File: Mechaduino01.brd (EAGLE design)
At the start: 42.9 x 43.2 mm, 57 parts, among them IC1 SAMD21G18A-AUT, IC2 AP2112K-3.3, Q1 2.5A/30V, Q2 NFET, U3 74AHC1G125, Y1 32,768Khz

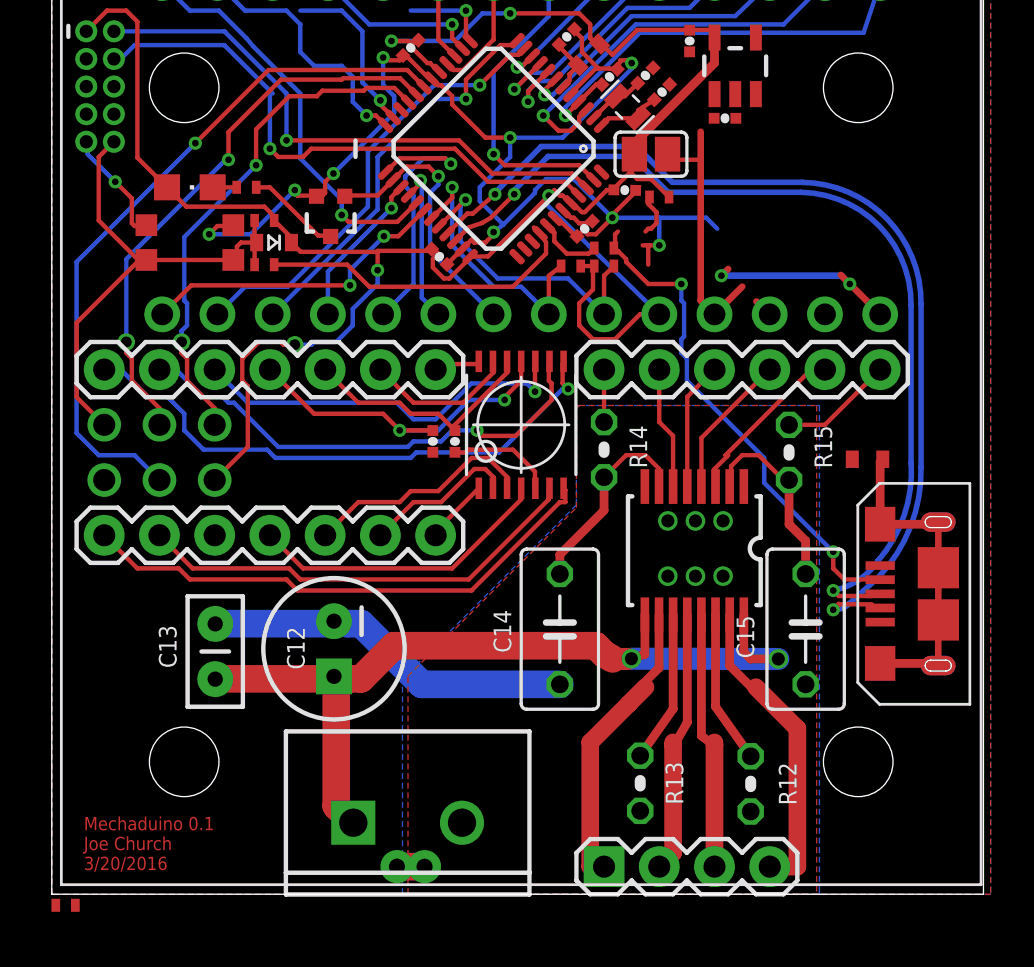
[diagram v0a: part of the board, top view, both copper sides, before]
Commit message: hardwired encoder, driver
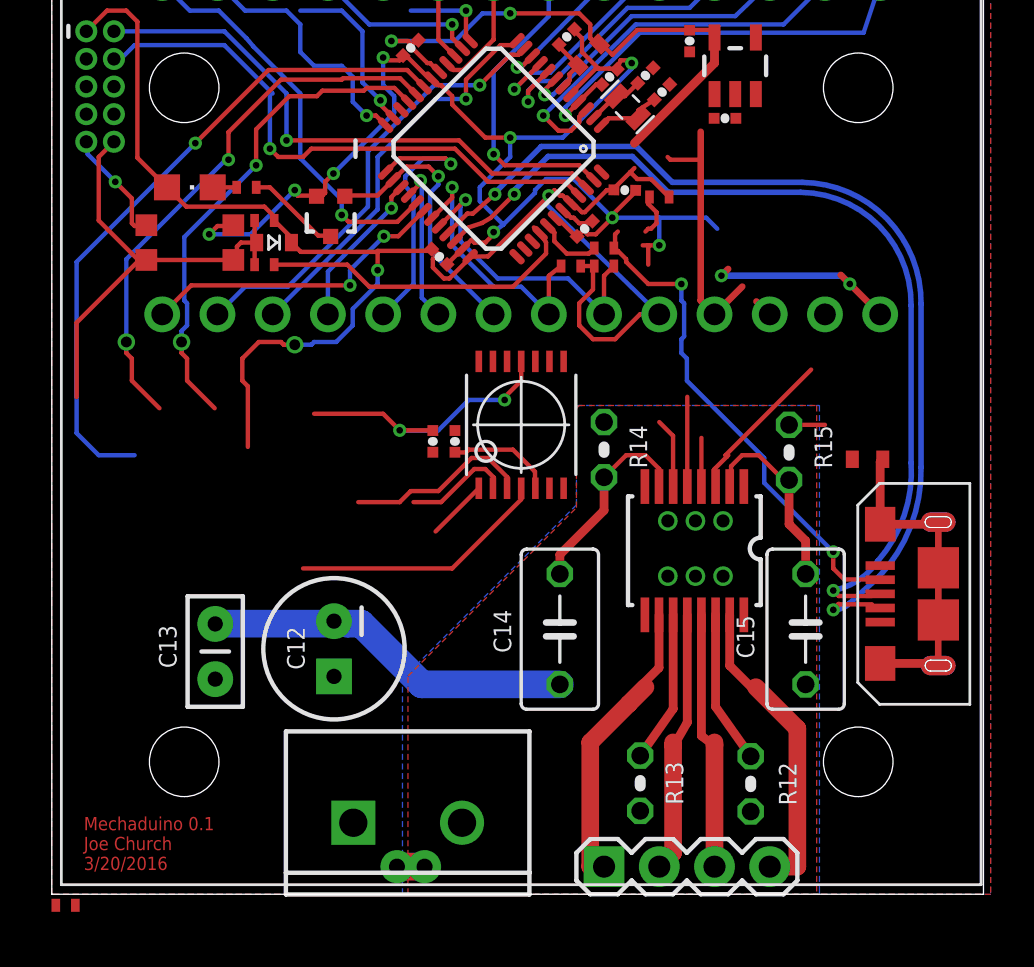
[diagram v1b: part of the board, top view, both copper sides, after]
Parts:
- removed JP10, JP11: (no value), SparkFun-Connectors:1X07
- removed JP3: SPI, Arduino-Neutrino-082:CONNETTORI_2X03
- removed JP5: (no value), SparkFun-Connectors:1X06
- removed SJ1: (no value), jumper:SJ
- renumbered POWERCONNECTOR to MOTOR_POWER
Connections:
- net N$5 renamed V+
- removed net ARDUINO_D4: IC1.13, JP1.12
- removed net ARDUINO_D5: IC1.24, JP1.13
- removed net ARDUINO_D6: IC1.29, JP1.14
- removed net ARDUINO_D7: IC1.30, JP2.1
- removed net ARDUINO_D8: IC1.11, JP2.2
- removed net ARDUINO_D9: IC1.12, JP2.3
- removed net N$10: JP5.4, U$1.5
- removed net N$11: JP5.5, U$1.6
- removed net N$12: JP5.6, R14.1
- removed net N$17: JP10.1, U$4.1
- removed net N$18: JP10.2, U$4.2
- removed net N$19: JP10.3, U$4.3
- removed net N$20: JP10.4, U$4.4
- removed net N$21: JP5.1, R15.1
- removed net N$22: JP10.6, U$4.6
- removed net N$23: JP10.7, U$4.7
- removed net N$24: JP11.1, U$4.8
- removed net N$25: JP11.2, U$4.9
- removed net N$26: JP11.3, U$4.10
- removed net N$28: C17.1, JP11.5, U$4.12
- removed net N$29: JP11.6, U$4.13
- removed net N$30: JP11.7, U$4.14
- removed net N$8: JP5.2, U$1.3
- removed net N$9: JP5.3, U$1.4
- removed net PB10_S4_SPI_MOSI: IC1.19, JP3.4
- removed net PB11_S4_SPI_SCK: IC1.20, JP3.3
- removed net PB12_S4_SPI_MISO: IC1.21, JP3.1
- new net ARDUINO_D4----VREF2: IC1.13, JP1.12, R15.1
- new net ARDUINO_D5----IN3: IC1.24, JP1.13, U$1.3
- new net ARDUINO_D6----IN4: IC1.29, JP1.14, U$1.4
- new net ARDUINO_D7----IN2: IC1.30, JP2.1, U$1.5
- new net ARDUINO_D8----IN1: IC1.11, JP2.2, U$1.6
- new net ARDUINO_D9----VREF1: IC1.12, JP2.3, R14.1
- new net HEADER_MISO: IC1.21, U$4.3
- new net HEADER_MOSI: IC1.19, U$4.4
- new net HEADER_SCK: IC1.20, U$4.2
- new net HEADER_SS: U$4.1
- net 3.3V: now also C17.1, U$4.12; no longer JP3.2, SJ1.2
- net GND: now also U$4.13; no longer JP10.5, JP3.6
- net N$27: no longer JP11.4
- net RESET: no longer JP3.5
- net VIN: no longer SJ1.1
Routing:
- net HEADER_MOSI: track 0.00 -> 42.8 mm, vias 0 -> 1
- net V+: track 39.8 -> 0.00 mm, vias 2 -> 0
- net PB10_S4_SPI_MOSI: track 32.5 -> 0.00 mm, vias 1 -> 0
- net HEADER_MISO: track 0.00 -> 31.6 mm, vias 0 -> 2
- net HEADER_SCK: track 0.00 -> 30.5 mm, vias 0 -> 2
- net PB11_S4_SPI_SCK: track 26.3 -> 0.00 mm, vias 2 -> 0
- net N$24: track 26.2 -> 0.00 mm, vias 1 -> 0
- net N$23: track 24.6 -> 0.00 mm
- net ARDUINO_D8----IN1: track 0.00 -> 23.9 mm, vias 0 -> 1
- net PB12_S4_SPI_MISO: track 23.8 -> 0.00 mm, vias 2 -> 0
- net N$25: track 22.4 -> 0.00 mm, vias 1 -> 0
- net ARDUINO_D6----IN4: track 0.00 -> 21.0 mm, vias 0 -> 1
- net N$22: track 20.8 -> 0.00 mm
- net ARDUINO_D8: track 20.7 -> 0.00 mm, vias 1 -> 0
- net ARDUINO_D5----IN3: track 0.00 -> 19.2 mm, vias 0 -> 1
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
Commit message: formatted and added license
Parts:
- added FRAME1: FRAME-LEDGER, SparkFun-Aesthetics:CREATIVE_COMMONS
- added LOGO4: OSHW-LOGOL, SparkFun-Aesthetics:OSHW-LOGO-L
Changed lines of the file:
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@@
 <attribute name="PROD_ID" value="IC-11920" x="-1.905" y="-18.542" size="1.778" layer="27" display="off"/>
 </element>
+<element name="FRAME1" library="SparkFun-Aesthetics" package="CREATIVE_COMMONS" value="FRAME-LEDGER" x="-88.16045625" y="0"/>
+<element name="LOGO4" library="SparkFun-Aesthetics" package="OSHW-LOGO-L" value="OSHW-LOGOL" x="-105.41" y="-37.465"/>
 </elements>
 <signals>

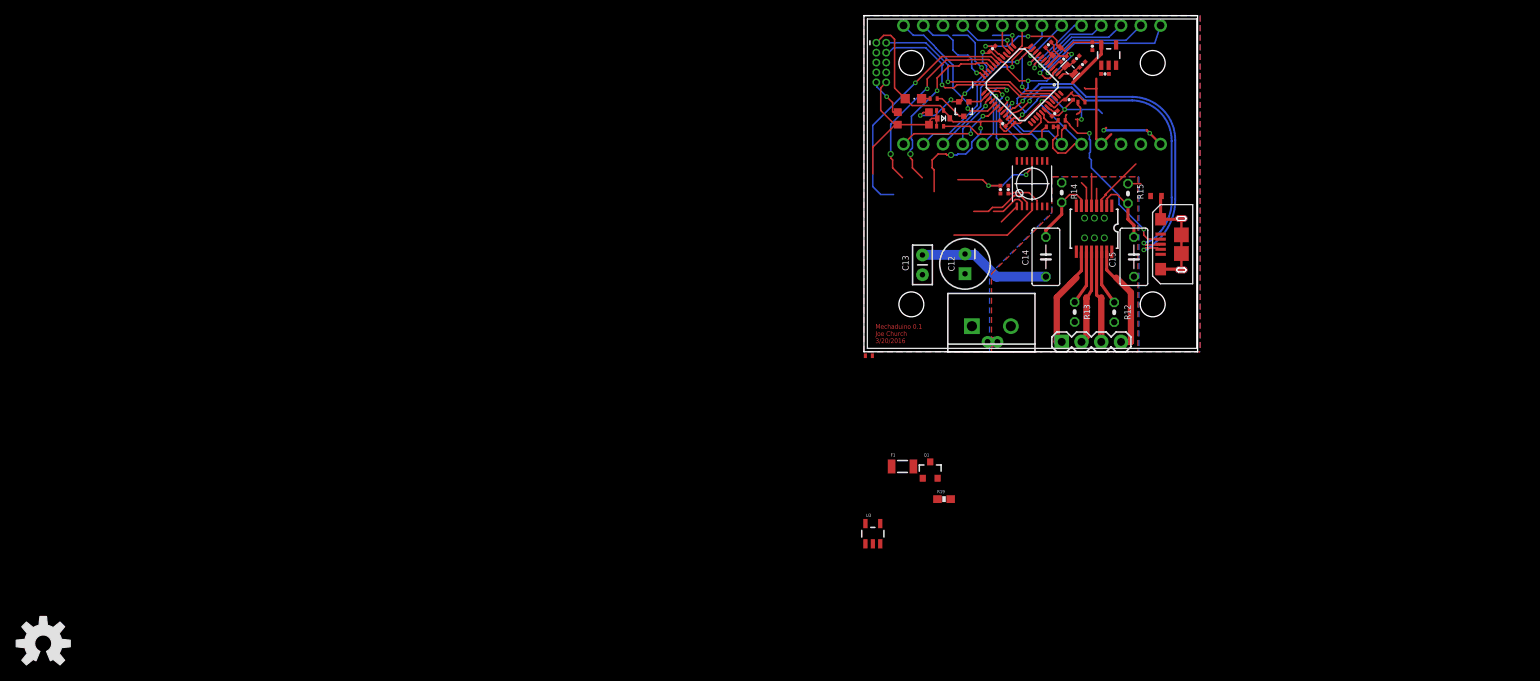
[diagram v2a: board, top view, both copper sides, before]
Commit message: ready for layout
ripped up old stuff, shrunk to 1.65" square from 1.7" and moved
placement sensitive parts accordingly
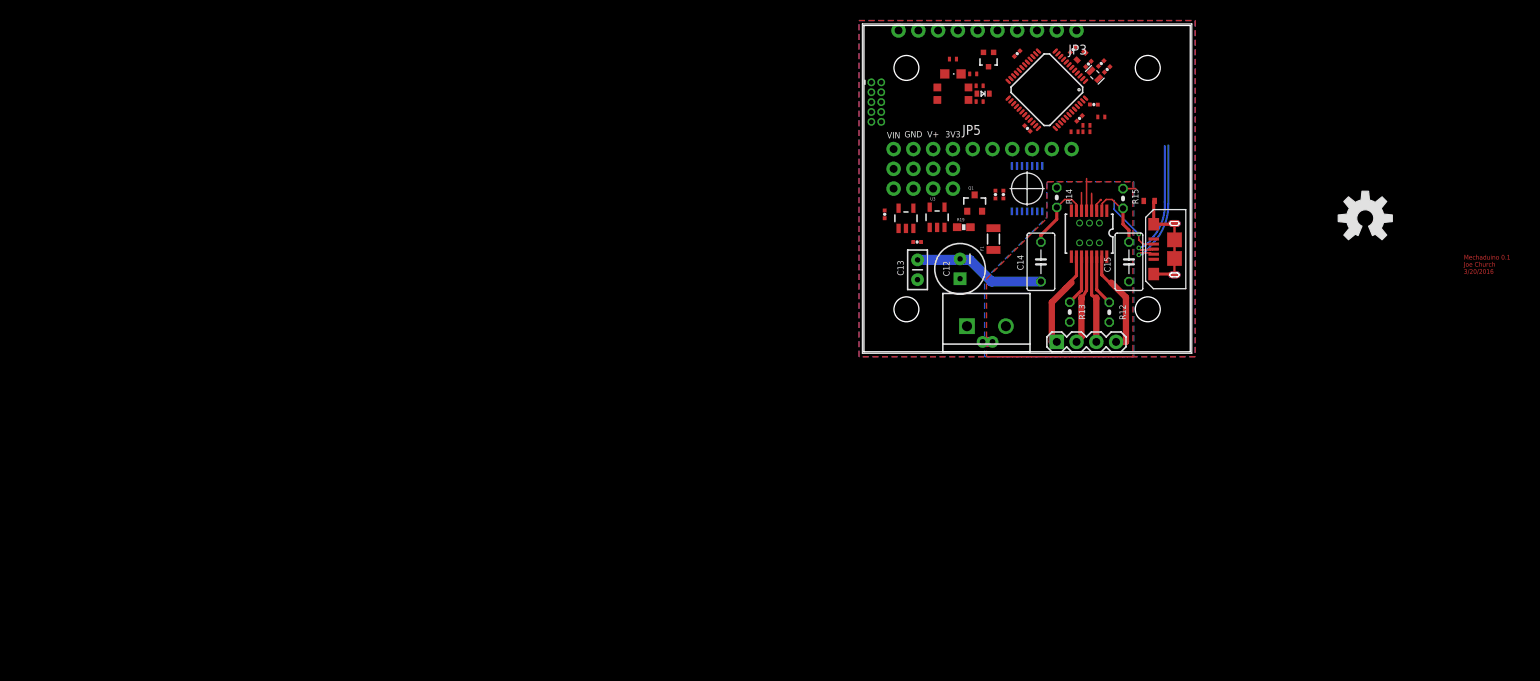
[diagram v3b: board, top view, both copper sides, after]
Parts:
- removed JP1, JP2: (no value), SparkFun-Connectors:1X14_NO_SILK_SMALLPADS
- added 3V3, GND, V+, VIN: (no value), SparkFun-Connectors:1X03_NO_SILK
- added JP3: (no value), SparkFun-Connectors:1X10_NO_SILK
- added JP5: (no value), SparkFun-Connectors:1X06_NO_SILK
- moved LOGO4 178.4 mm to (64.4, 17.1)
- moved FRAME1 89.4 mm to (0.61, -10.4)
- moved U$3 49.5 mm to (62.5, 11.3)
- moved U3 41.5 mm to (9.40, 17.3)
- moved R16 39.6 mm to (11.4, 37.6)
- moved R19 35.0 mm to (12.8, 16.0)
- moved Q1 34.8 mm to (14.2, 19.1)
- moved C10 34.3 mm to (2.67, 17.7)
- moved IC2 33.4 mm to (5.40, 17.1)
- moved C9 32.4 mm to (6.83, 14.1)
- moved F1 31.5 mm to (16.6, 14.5), turned to 90 degrees
- moved Q2 7.10 mm to (16.0, 37.5)
- moved R6 5.99 mm to (14.9, 32.1)
- moved D1 5.99 mm to (15.3, 33.1)
- moved LED1 5.99 mm to (11.4, 35.7)
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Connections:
- removed net ARDUINO_A2: IC1.8, JP1.4
- removed net HEADER_SS: U$4.1
- removed net VBUS: JP2.12
- removed net VOUT: JP2.11
- new net ARDUINO_A2----HEADER_SS: IC1.8, U$4.1
- net 3.3V: now also 3V3.1, 3V3.2, 3V3.3; no longer JP2.10
- net ARDUINO_A0: now also JP3.2; no longer JP1.2
- net ARDUINO_A1: now also JP3.3; no longer JP1.3
- net ARDUINO_A3: now also JP3.4; no longer JP1.5
- net ARDUINO_A4: now also JP3.5; no longer JP1.6
- net ARDUINO_A5: now also JP3.6; no longer JP1.7
- net ARDUINO_AREF: now also JP3.1; no longer JP1.1
- net ARDUINO_D0: now also JP3.7; no longer JP1.8
- net ARDUINO_D1: now also JP3.8; no longer JP1.9
- net ARDUINO_D10_SS: now also JP5.1; no longer JP2.4
- net ARDUINO_D11_MOSI: now also JP5.2; no longer JP2.5
- net ARDUINO_D12_MISO: now also JP5.3; no longer JP2.6
- net ARDUINO_D13_SCK: now also JP5.4; no longer JP2.7
- net ARDUINO_D2: now also JP3.9; no longer JP1.10
- net ARDUINO_D20_SDA: now also JP5.5; no longer JP2.8
- net ARDUINO_D21_SCL: now also JP5.6; no longer JP2.9
- net ARDUINO_D3: now also JP3.10; no longer JP1.11
- net ARDUINO_D4----VREF2: no longer JP1.12
- net ARDUINO_D5----IN3: no longer JP1.13
- net ARDUINO_D6----IN4: no longer JP1.14
- net ARDUINO_D7----IN2: no longer JP2.1
- net ARDUINO_D8----IN1: no longer JP2.2
- net ARDUINO_D9----VREF1: no longer JP2.3
- net GND: now also GND.1, GND.2, GND.3; no longer JP2.13
- net V+: now also V+.1, V+.2, V+.3
- net VIN: now also VIN.1, VIN.2, VIN.3; no longer JP2.14
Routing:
- net 3.3V: track 97.3 -> 0.00 mm, vias 5 -> 0
- net GND: track 75.3 -> 0.00 mm, vias 10 -> 0
- net HEADER_MOSI: track 42.8 -> 0.00 mm, vias 1 -> 0
- net HEADER_MISO: track 31.6 -> 0.00 mm, vias 2 -> 0
- net HEADER_SCK: track 30.5 -> 0.00 mm, vias 2 -> 0
- net TARGET_USB_N: track 44.6 -> 17.4 mm, vias 2 -> 1
- net PA30_SWCLK: track 26.5 -> 0.00 mm, vias 1 -> 0
- net TARGET_USB_P: track 42.5 -> 16.4 mm, vias 2 -> 1
- net PA31_SWDIO: track 26.0 -> 0.00 mm, vias 1 -> 0
- net RESET: track 22.6 -> 0.00 mm
- net ARDUINO_D8----IN1: track 23.9 -> 2.33 mm, vias 1 -> 0
- net ARDUINO_AREF: track 20.2 -> 0.00 mm, vias 1 -> 0
- net ARDUINO_D6----IN4: track 21.0 -> 2.24 mm, vias 1 -> 0
- net ARDUINO_D9----VREF1: track 18.4 -> 0.00 mm, vias 1 -> 0
- net ARDUINO_A0: track 18.3 -> 0.00 mm, vias 1 -> 0
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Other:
- board size 42.9 x 43.2 mm -> 41.9 x 41.9 mm
- board text added: "Joe Church"
- board text removed: "A"
- board text removed: "B"
- board text removed: "CLK"
- board text removed: "CSN"
- board text removed: "I"
- board text removed: "IN1"
- board text removed: "IN2"
- board text removed: "IN3"
- board text removed: "IN4"
- board text removed: "MISO"
- board text removed: "MOSI"
- board text removed: "SCK"
- board text removed: "SPI"
- board text removed: "TEST"
- board text removed: "U"
- board text removed: "V"
- board text removed: "VDD"
- board text removed: "VDD3V"
- board text removed: "VREF12"
- board text removed: "VREF34"
- board text removed: "W"

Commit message: added level shifter
on D0, D1
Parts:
- added Q3, Q4: BSS138, SparkFun:SOT23-3
- added R2, R20, R21, R3: 10K, adafruit:R0402-VISHAY
- moved GND 1.42 mm to (7.62, 26.7)
- moved VIN 1.42 mm to (5.08, 26.7)
- moved 3V3 1.42 mm to (12.7, 26.7)
- moved JP5 1.42 mm to (15.2, 26.7)
- moved V+ 1.42 mm to (10.2, 26.7)
- moved JP4 1.27 mm to (1.59, 30.8)
- moved JP3 0.90 mm to (27.9, 40.6)
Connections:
- new net HV1: JP3.8, Q3.3, R21.1
- new net HV2: JP3.7, Q4.3, R2.1
- net 3.3V: now also Q3.1, Q4.1, R20.2, R3.2
- net ARDUINO_D0: now also Q4.2, R3.1; no longer JP3.7
- net ARDUINO_D1: now also Q3.2, R20.1; no longer JP3.8
- net VIN: now also R2.2, R21.2

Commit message: cut corners
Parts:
- moved 3V3 3.81 mm to (16.5, 26.7)
- moved JP5 3.81 mm to (19.1, 26.7)
- moved V+ 3.81 mm to (14.0, 26.7)
- moved VIN 3.81 mm to (8.89, 26.7)
- moved GND 3.81 mm to (11.4, 26.7)
- moved JP3 3.81 mm to (31.8, 40.6)
- moved C16 1.27 mm to (16.9, 18.9)
- moved C17 1.27 mm to (17.9, 18.9)
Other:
- outline, holes or cut-outs redrawn

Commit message: cut corners...
resaved
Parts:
- moved U$3 11.5 mm to (70.9, 19.2), turned to 0 degrees
- moved LOGO4 6.48 mm to (58.0, 18.4)
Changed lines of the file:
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@@
 <grid distance="0.05" unitdist="inch" unit="inch" style="lines" multiple="1" display="yes" altdistance="0.025" altunitdist="inch" altunit="inch"/>
 <layers>
-<layer number="1" name="Top" color="4" fill="1" visible="no" active="yes"/>
-<layer number="16" name="Bottom" color="1" fill="1" visible="no" active="yes"/>
-<layer number="17" name="Pads" color="2" fill="1" visible="no" active="yes"/>
-<layer number="18" name="Vias" color="2" fill="1" visible="no" active="yes"/>
+<layer number="1" name="Top" color="4" fill="1" visible="yes" active="yes"/>
+<layer number="16" name="Bottom" color="1" fill="1" visible="yes" active="yes"/>
+<layer number="17" name="Pads" color="2" fill="1" visible="yes" active="yes"/>
+<layer number="18" name="Vias" color="2" fill="1" visible="yes" active="yes"/>
 <layer number="19" name="Unrouted" color="15" fill="1" visible="yes" active="yes"/>
 <layer number="20" name="Dimension" color="15" fill="1" visible="yes" active="yes"/>
@@
 <attribute name="NAME" x="15.494" y="2.159" size="0.762" layer="51" ratio="10" rot="R270"/>
 </element>
-<element name="U$3" library="stepper_servo_prototype_1" package="LOGO2" value="TROPICAL_LABS_LOGO_1LOGO2" x="62.484" y="11.303" rot="MR180"/>
+<element name="U$3" library="stepper_servo_prototype_1" package="LOGO2" value="TROPICAL_LABS_LOGO_1LOGO2" x="70.866" y="19.177" rot="MR0"/>
 <element name="J1" library="MF_Connectors" package="MICROUSB-RIGHT" value="" x="38.481" y="13.181" smashed="yes" rot="R90"/>
 <element name="R16" library="adafruit" package="R0402-VISHAY" value="100k" x="11.43" y="37.592"/>
@@
 </element>
 <element name="FRAME1" library="SparkFun-Aesthetics" package="CREATIVE_COMMONS" value="FRAME-LEDGER" x="0.61254375" y="-10.414" smashed="yes"/>
-<element name="LOGO4" library="SparkFun-Aesthetics" package="OSHW-LOGO-L" value="OSHW-LOGOL" x="64.389" y="17.145"/>
+<element name="LOGO4" library="SparkFun-Aesthetics" package="OSHW-LOGO-L" value="OSHW-LOGOL" x="58.039" y="18.415"/>
 <element name="JP3" library="SparkFun-Connectors" package="1X10_NO_SILK" value="" x="31.75" y="40.64" rot="R180">
 <attribute name="PROD_ID" value="CONN-11563" x="31.75" y="40.64" size="1.778" layer="27" rot="R180" display="off"/>
